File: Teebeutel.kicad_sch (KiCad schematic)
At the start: 163 parts, among them J1 Conn_01x10_Female, J2 Conn_01x10_Female, J3 Micro_SD_Card, J4 RJ45_Shielded, J5 Conn_01x30_Female, J6 Battery, M1 Motor_DC, Q1 S8050, Q2 AO3400, Q3 AO3400, Q4 S8050, Q5 AO3400, Q6 AO3400, Q7 AO3400, SW1 K1-1506SN-01, SW2 SW_SPST, U1 SDB628, U10 TLV70018_SOT23-5, U11 TLV62569DBVR, U12 MCP73831-2-OT, U2 RM-V8xxC_TR1, U3 PCA9539BS,118, U4 TXB0104RUT, U5 ESP32-WROOM-32E(16MB), U6 SRV05-4, U7 SGP30, U8 PPSI262, U9 LIS2DE12

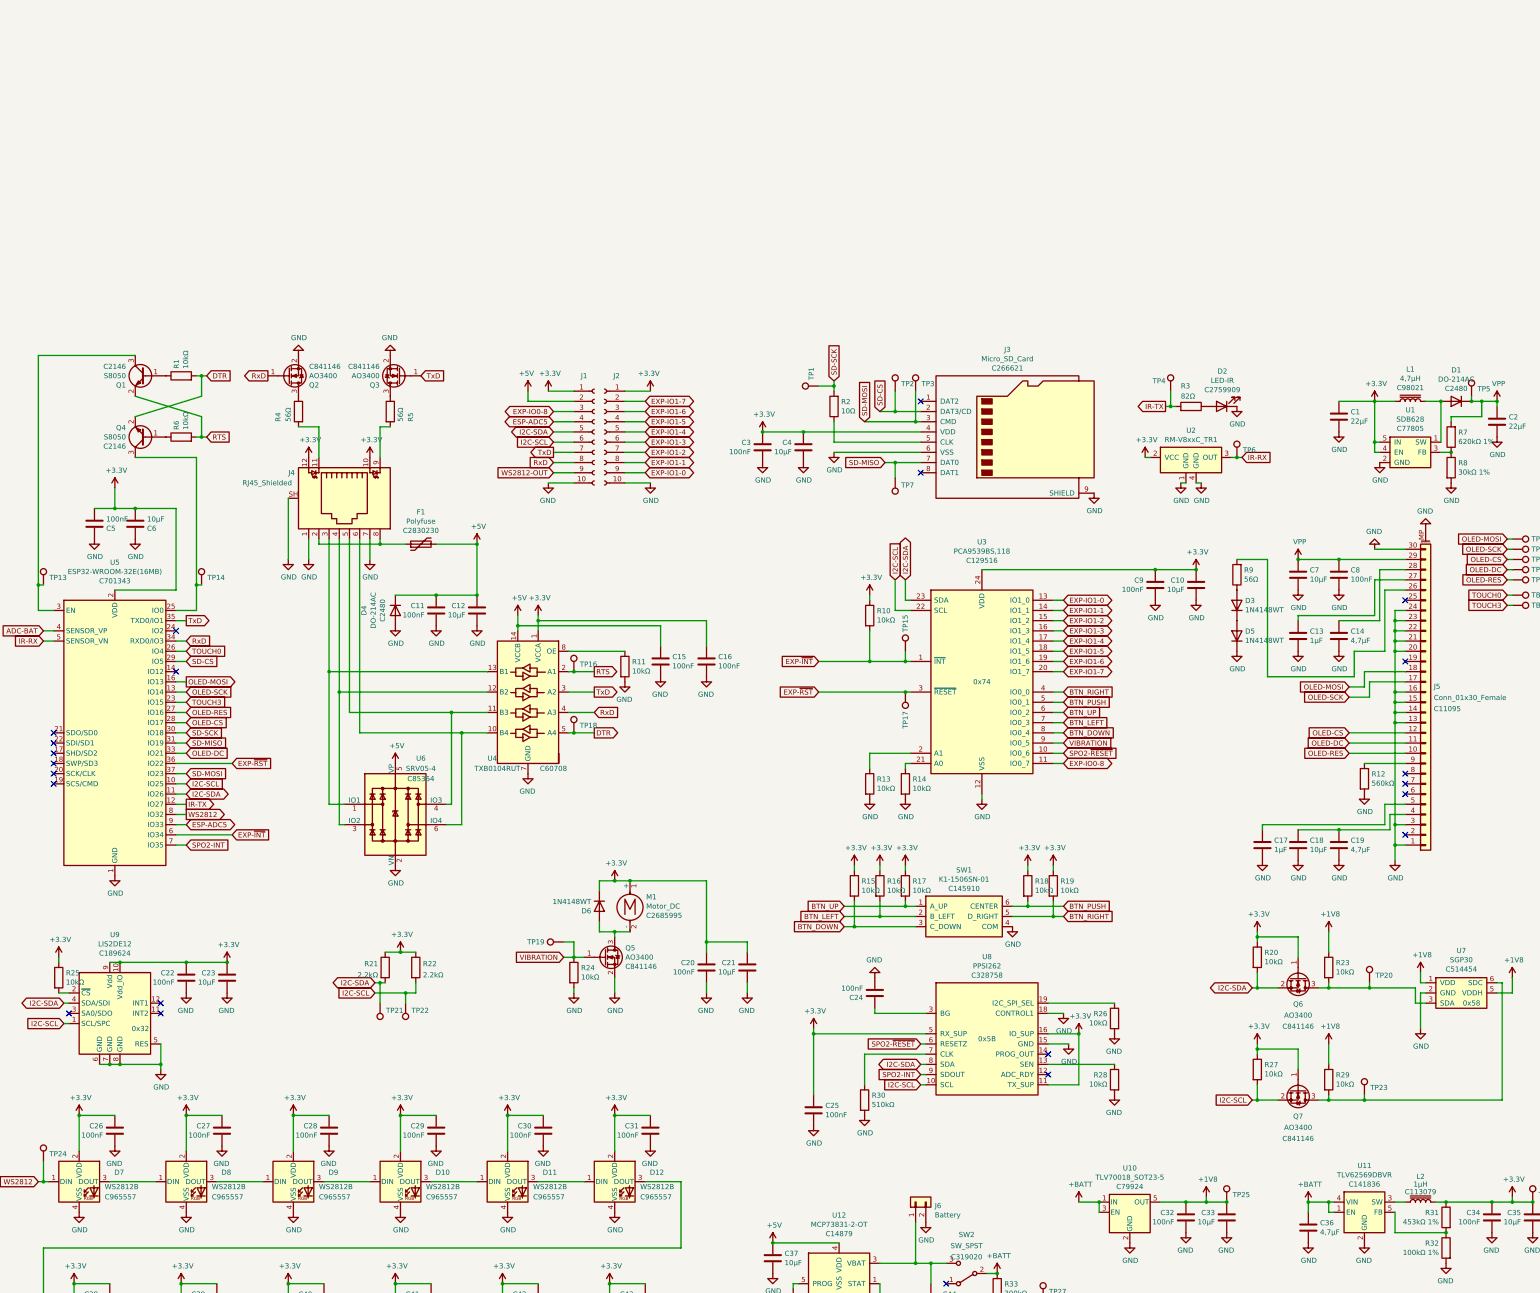
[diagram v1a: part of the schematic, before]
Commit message: feat(): Add USB-Adaptor
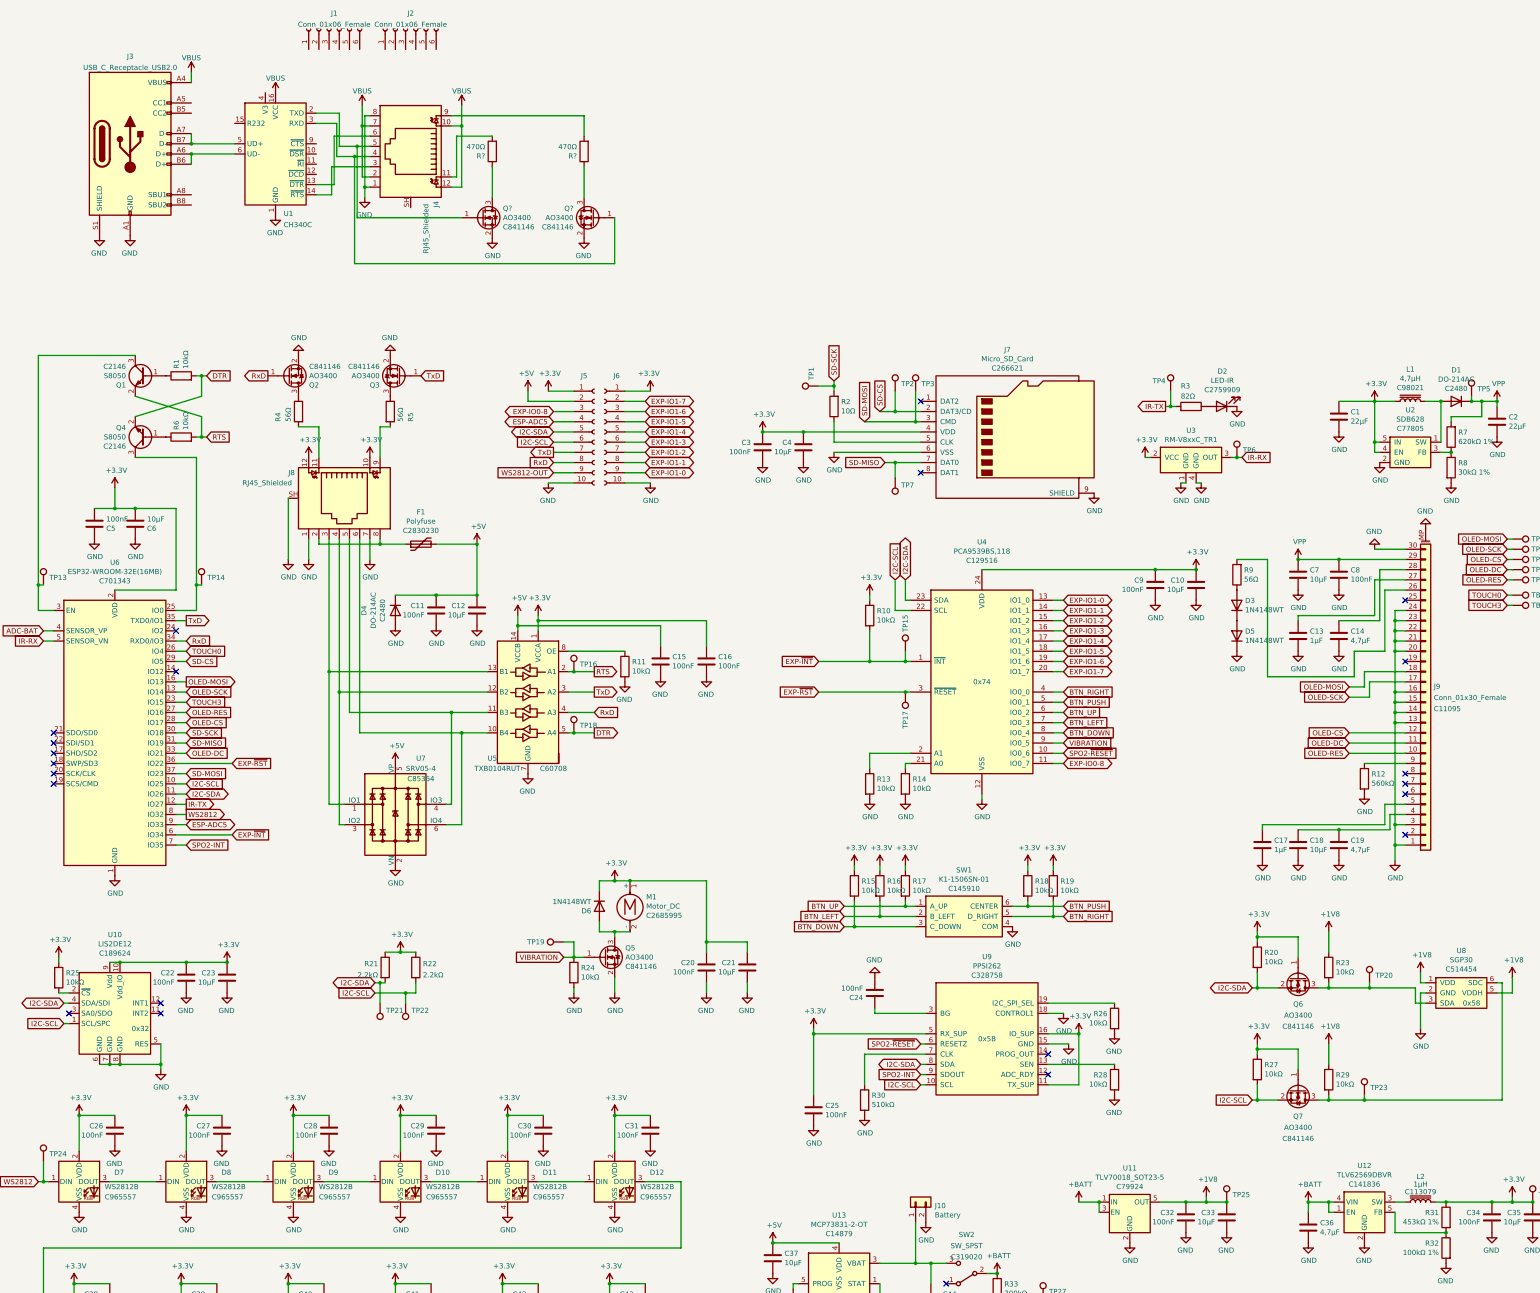
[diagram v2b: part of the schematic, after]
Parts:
- added J1: Conn_01x06_Female, Connector_PinSocket_2.54mm:PinSocket_1x06_P2.54mm_Vertical_SMD_Pin1Right, symbol Connector:Conn_01x06_Female
- added J2: Conn_01x06_Female, Connector_PinSocket_2.54mm:PinSocket_1x06_P2.54mm_Vertical_SMD_Pin1Left, symbol Connector:Conn_01x06_Female
- added J3: USB_C_Receptacle_USB2.0, Connector_USB:USB_C_Receptacle_Palconn_UTC16-G, symbol Connector:USB_C_Receptacle_USB2.0
- added J4: RJ45_Shielded, Connector_RJ:RJ45_Amphenol_RJHSE538X, symbol Connector:RJ45_LED_Shielded
- added Q? (x2): AO3400, Package_TO_SOT_SMD:SOT-23, symbol Transistor_FET:BSN20
- added R? (x2): 470Ω, Resistor_SMD:R_0603_1608Metric, symbol Device:R
- added U1: CH340C, Package_SO:SOIC-16_3.9x9.9mm_P1.27mm, symbol Interface_USB:CH340C
- renumbered J6 to J10, J1 to J5, J2 to J6, J3 to J7, J4 to J8, J5 to J9, U9 to U10, U10 to U11, U11 to U12, U12 to U13, U1 to U2, U2 to U3, U3 to U4, U4 to U5, U5 to U6, U6 to U7, U7 to U8, U8 to U9
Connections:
- net GND: now also J3.A1 (GND), J3.A12 (GND), J3.B1 (GND), J3.B12 (GND), J3.S1 (SHIELD), J4.1, J4.8, Q?.2 (S), Q?.2 (S), U1.1 (GND)
- new net: J4.11, R?.2
- new net: J4.3, U1.14 (~{RTS})
- new net: J4.4, Q?.1 (G), U1.3 (RXD)
- new net: J4.5, Q?.1 (G), U1.2 (TXD)
- new net: J4.6, U1.13 (~{DTR})
- new net: J4.9, R?.2
- new net: Q?.3 (D), R?.1 (x2)
- new net: J3.A6 (D+), J3.B6 (D+), U1.6 (UD-)
- new net: J3.A7 (D-), J3.B7 (D-), U1.5 (UD+)
- new net VBUS: J3.A4 (VBUS), J3.A9 (VBUS), J3.B4 (VBUS), J3.B9 (VBUS), J4.10, J4.12, J4.2, J4.7, U1.16 (VCC)

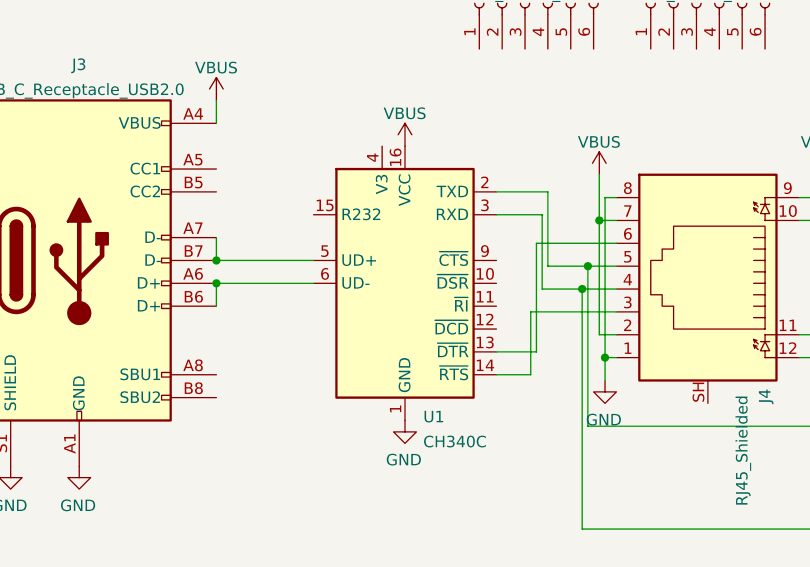
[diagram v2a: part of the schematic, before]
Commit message: feat(): Add USB-Adaptor
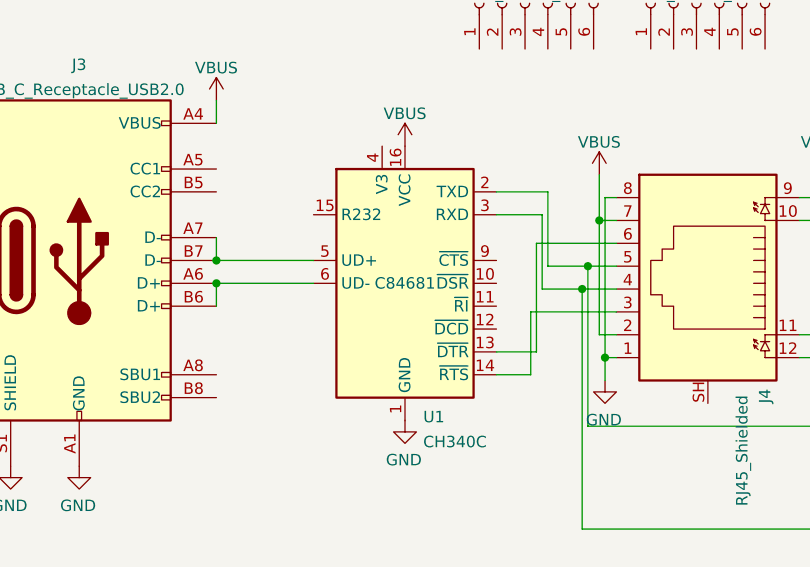
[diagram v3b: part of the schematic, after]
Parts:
- U1: LCSC (none) -> C84681
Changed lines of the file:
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@@
       (effects (font (size 1.27 1.27)) hide)
     )
+    (property "LCSC" "C84681" (id 4) (at 86.995 -31.115 0))
     (pin "1")
     (pin "10")

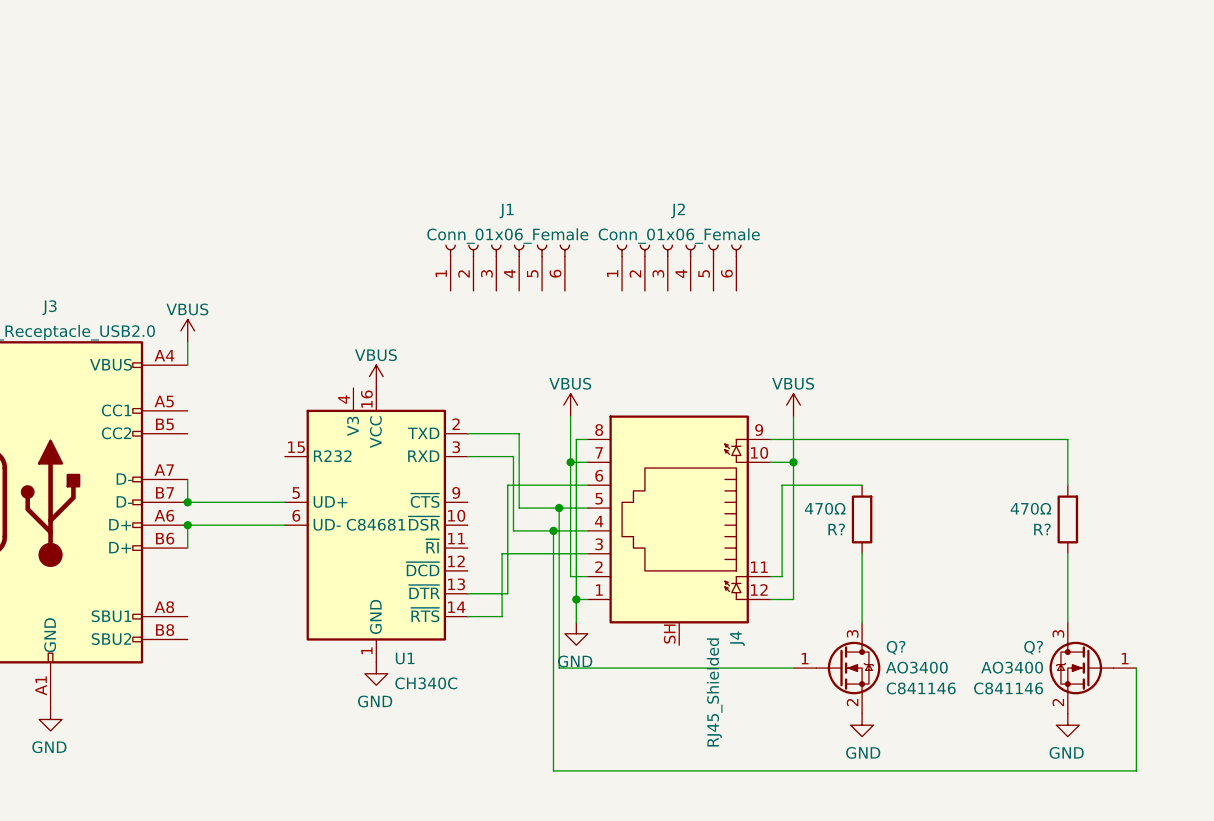
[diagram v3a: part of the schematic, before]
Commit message: Schematic: Added capacitors to CH340C
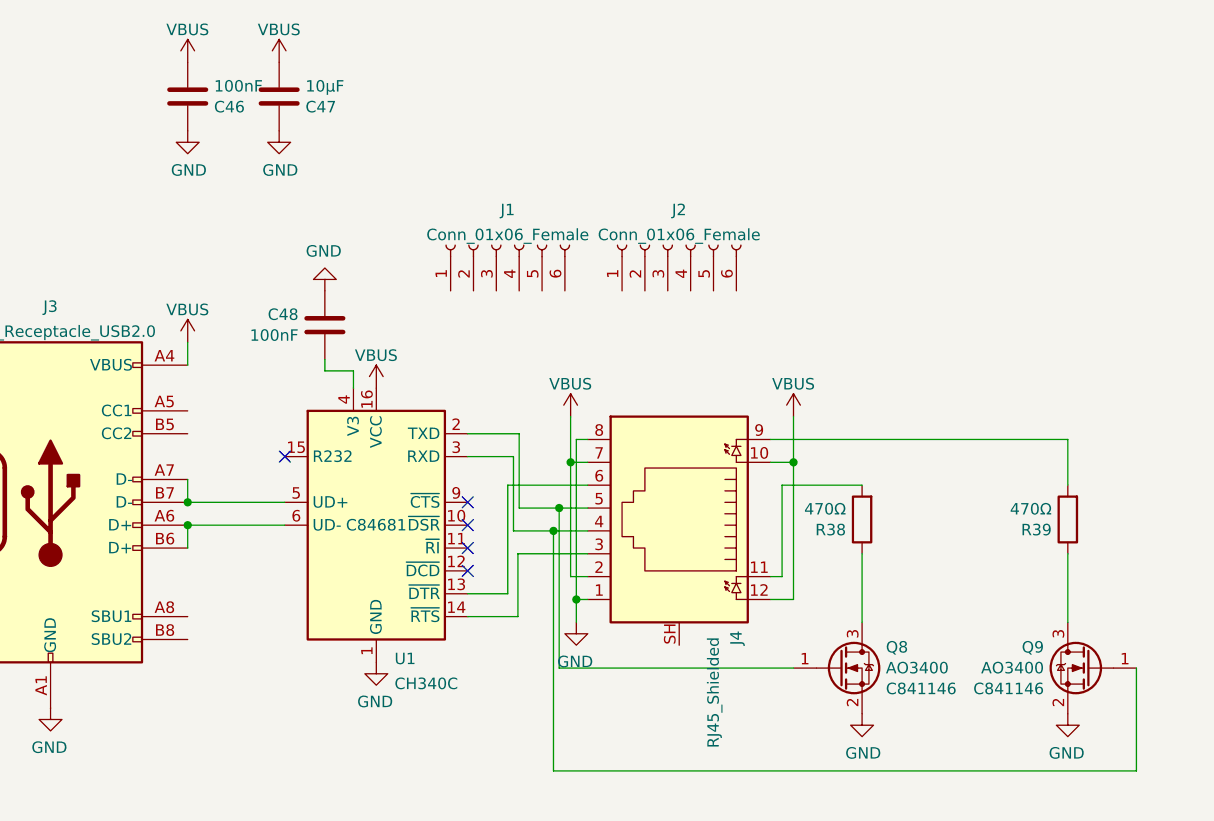
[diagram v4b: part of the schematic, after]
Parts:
- added C46, C48: 100nF, Capacitor_SMD:C_0603_1608Metric, symbol Device:C
- added C47: 10µF, Capacitor_SMD:C_0603_1608Metric, symbol Device:C
- gave numbers to parts that had none: 4
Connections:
- net GND: now also C46.1, C47.1, C48.1
- net VBUS: now also C46.2, C47.2
- net at U1.4 (V3): now also C48.2
- no-connect marks 22 -> 27

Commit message: feat(): Add fuse and finalize USB-Adaptor
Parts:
- removed C46, C48: 100nF, Capacitor_SMD:C_0603_1608Metric, symbol Device:C
- removed C47: 10µF, Capacitor_SMD:C_0603_1608Metric, symbol Device:C
- removed J1: Conn_01x06_Female, Connector_PinSocket_2.54mm:PinSocket_1x06_P2.54mm_Vertical_SMD_Pin1Right, symbol Connector:Conn_01x06_Female
- removed J3: USB_C_Receptacle_USB2.0, Connector_USB:USB_C_Receptacle_Palconn_UTC16-G, symbol Connector:USB_C_Receptacle_USB2.0
- removed J4: RJ45_Shielded, Connector_RJ:RJ45_Amphenol_RJHSE538X, symbol Connector:RJ45_LED_Shielded
- removed Q8, Q9: AO3400, Package_TO_SOT_SMD:SOT-23, symbol Transistor_FET:BSN20
- removed R38, R39: 470Ω, Resistor_SMD:R_0603_1608Metric, symbol Device:R
- added C1, C3: 100nF, Capacitor_SMD:C_0603_1608Metric, symbol Device:C
- added C2: 10µF, Capacitor_SMD:C_0603_1608Metric, symbol Device:C
- added F2: Polyfuse, Fuse:Fuse_0805_2012Metric, symbol Device:Polyfuse
- added J1: USB_A, Teebeutel_Special_Parts:on-pcb-USB-A, symbol Connector:USB_A
- added J3: Conn_01x06_Female, Connector_PinSocket_2.54mm:PinSocket_1x06_P2.54mm_Vertical_SMD_Pin1Left, symbol Connector:Conn_01x06_Female
- added J4: USB_C_Receptacle_USB2.0, Connector_USB:USB_C_Receptacle_Palconn_UTC16-G, symbol Connector:USB_C_Receptacle_USB2.0
- added J5: RJ45_Shielded, Connector_RJ:RJ45_Amphenol_RJHSE538X, symbol Connector:RJ45_LED_Shielded
- added Q1, Q2: AO3400, Package_TO_SOT_SMD:SOT-23, symbol Transistor_FET:BSN20
- added R1, R2: 470Ω, Resistor_SMD:R_0603_1608Metric, symbol Device:R
- J2: footprint Connector_PinSocket_2.54mm:PinSocket_1x06_P2.54mm_Vertical_SMD_Pin1Left -> Connector_PinSocket_2.54mm:PinSocket_1x06_P2.54mm_Vertical_SMD_Pin1Right
- renumbered C7 to C10, C8 to C11, C9 to C12, C10 to C13, C11 to C14, C12 to C15, C13 to C16, C14 to C17, C15 to C18, C16 to C19, C17 to C20, C18 to C21, C19 to C22, C20 to C23, C21 to C24, C22 to C25, C23 to C26, C24 to C27, C25 to C28, C26 to C29, C27 to C30, C28 to C31, C29 to C32, C30 to C33, C31 to C34, C32 to C35, C33 to C36, C34 to C37, C35 to C38, C36 to C39, C1 to C4, C37 to C40, C38 to C41, C39 to C42, C40 to C43, C41 to C44, C42 to C45, C43 to C46, C44 to C47, C45 to C48, C2 to C5, C3 to C6, C4 to C7, C5 to C8, C6 to C9, J9 to J10, J10 to J11, J5 to J6, J6 to J7, J7 to J8, J8 to J9, Q1 to Q3, Q2 to Q4, Q3 to Q5, Q4 to Q6, Q5 to Q7, Q6 to Q8, Q7 to Q9, R8 to R10, R9 to R11, R10 to R12, R11 to R13, R12 to R14, R13 to R15, R14 to R16, R15 to R17, R16 to R18, R17 to R19, R18 to R20, R19 to R21, R20 to R22, R21 to R23, R22 to R24, R23 to R25, R24 to R26, R25 to R27, R26 to R28, R27 to R29, R1 to R3, R28 to R30, R29 to R31, R30 to R32, R31 to R33, R32 to R34, R33 to R35, R34 to R36, R35 to R37, R36 to R38, R37 to R39, R2 to R4, R3 to R5, R4 to R6, R5 to R7, R6 to R8, R7 to R9
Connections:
- net GND: now also J2.6 (Pin_6), C1.1, C2.1, C3.1, J1.4 (GND), J1.5 (Shield), J3.6 (Pin_6), J4.A1 (GND), J4.A12 (GND), J4.B1 (GND), J4.B12 (GND), J4.S1 (SHIELD), J5.1, J5.7, J5.SH, Q1.2 (S), Q2.2 (S)
- net VBUS: now also J2.1 (Pin_1), C1.2, C2.2, J1.1 (VBUS), J3.1 (Pin_1), J4.A4 (VBUS), J4.A9 (VBUS), J4.B4 (VBUS), J4.B9 (VBUS), J5.10, J5.12, J5.2, J5.8
- net at C47.1, SW2.3 (C), U13.3 (VBAT): now also F2.1; no longer J11.1 (Pin_1)
- net USB-~{RTS}: now reaches U1.14 (~{RTS})
- net USB-~{RTS}: now also J3.3 (Pin_3), J5.3
- net USB-RXD: now reaches U1.3 (RXD)
- net USB-RXD: now also J2.2 (Pin_2), J5.4, Q1.1 (G)
- net USB-TXD: now reaches U1.2 (TXD)
- net USB-TXD: now also J3.2 (Pin_2), J5.5, Q2.1 (G)
- net USB-~{DTR}: now reaches U1.13 (~{DTR})
- net USB-~{DTR}: now also J3.4 (Pin_4), J5.6
- net USB-D-: now reaches U1.6 (UD-)
- net USB-D-: now also J1.2 (D-), J4.A7 (D-), J4.B7 (D-)
- net USB-D+: now reaches U1.5 (UD+)
- net USB-D+: now also J1.3 (D+), J4.A6 (D+), J4.B6 (D+)
- net USB-~{CTS}: now reaches J2.3 (Pin_3)
- net USB-~{CTS}: now also U1.9 (~{CTS})
- net USB-~{DSR}: now reaches J2.4 (Pin_4)
- net USB-~{DSR}: now also U1.10 (~{DSR})
- net USB-~{RI}: now reaches J2.5 (Pin_5)
- net USB-~{RI}: now also U1.11 (~{RI})
- net USB-~{DCD}: now reaches U1.12 (~{DCD})
- net USB-~{DCD}: now also J3.5 (Pin_5)
- net at U1.4 (V3): now also C3.2
- new net: F2.2, J11.1 (Pin_1)
- new net: Q1.3 (D), R1.1
- new net: Q2.3 (D), R2.1
- new net: J5.11, R2.2
- new net: J5.9, R1.2
- no-connect marks 27 -> 23
